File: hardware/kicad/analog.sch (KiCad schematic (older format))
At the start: 0 parts

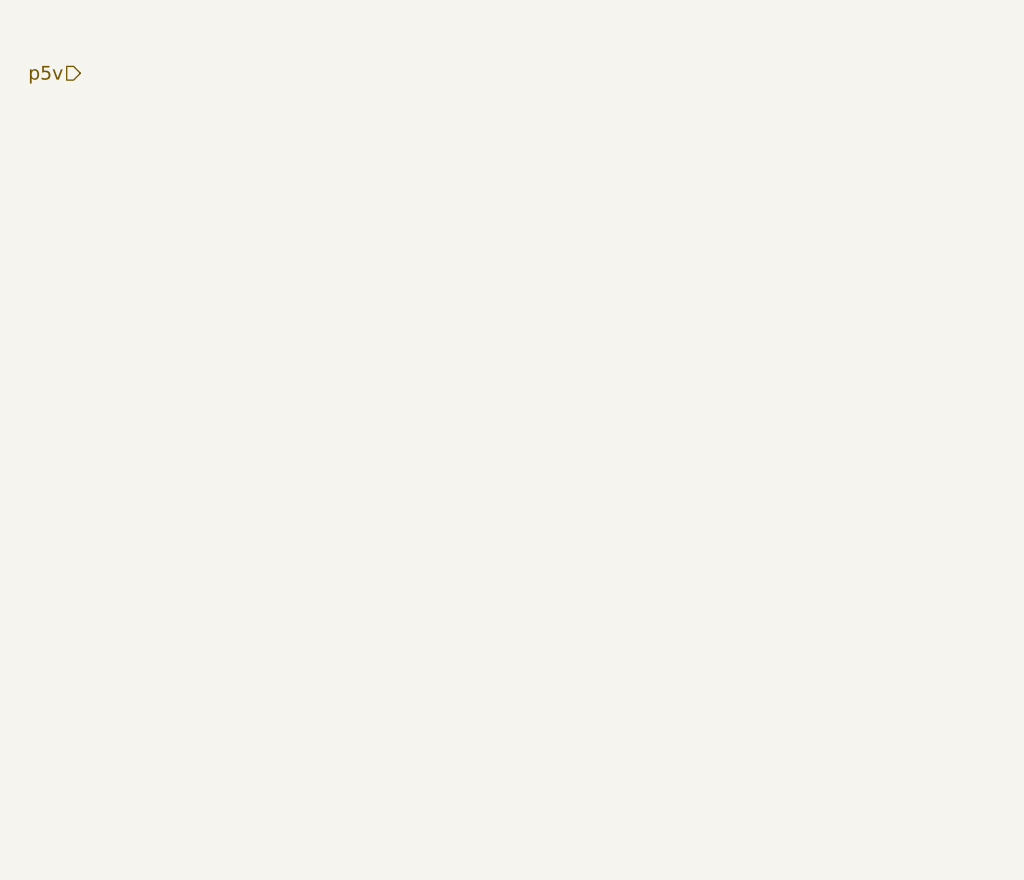
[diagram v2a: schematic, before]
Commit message: Updated schematic and Modex library.
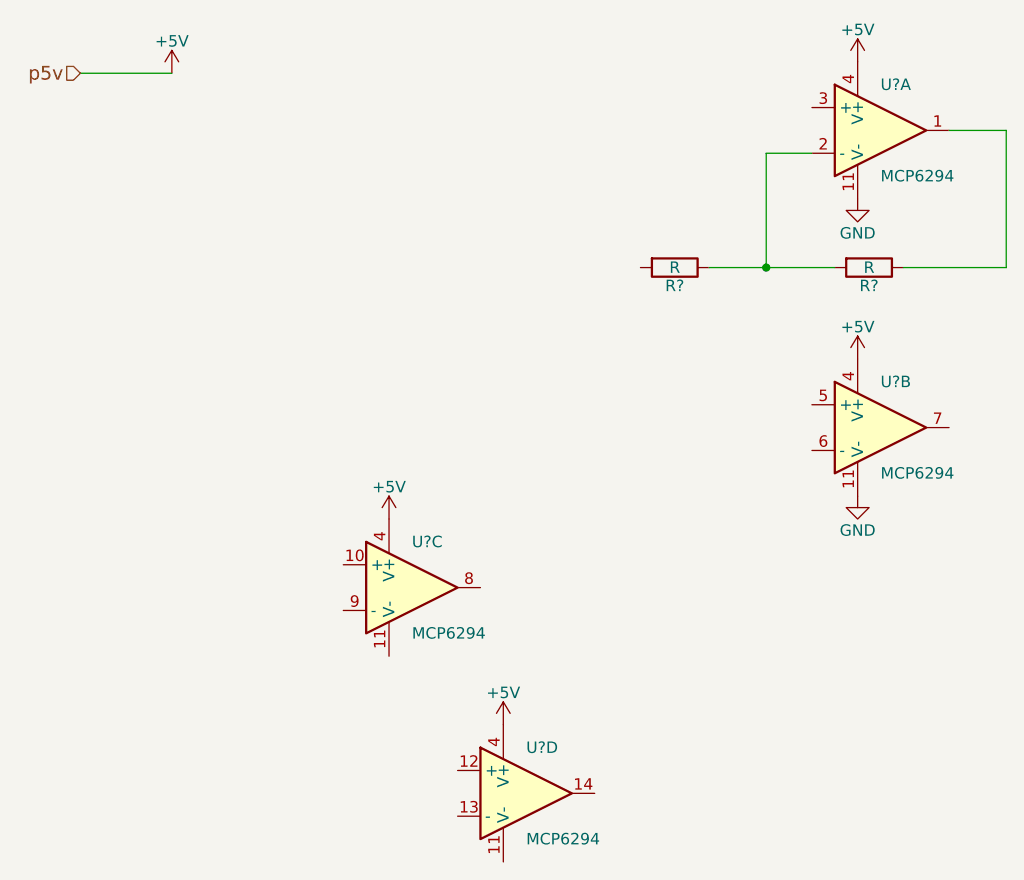
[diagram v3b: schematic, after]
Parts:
- added R? (x2): R, symbol R
- added U?: MCP6294, SMD_Packages:SO-16-N, symbol MCP6294
- added U? (x3): MCP6294, symbol MCP6294
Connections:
- new net: R?.1, U?.1
- new net: R?.1, R?.2, U?.2 (-)
- new net +5V: U?.4 (V+), U?.4 (V+), U?.4 (V+), U?.4 (V+)
- new net GND: U?.11 (V-), U?.11 (V-)
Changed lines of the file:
@@
 Text HLabel 2350 1750 0    60   Input ~ 0
 p5v
+$Comp
+L MCP6294 U?
+U 1 1 5803942A
+P 5850 2000
+F 0 "U?" H 5850 2200 50  0000 L CNN
+F 1 "MCP6294" H 5850 1800 50  0000 L CNN
+F 2 "SMD_Packages:SO-16-N" H 6500 2250 50  0001 C CNN
+F 3 "" H 5900 2200 50  0000 C CNN
+	1    5850 2000
+	1    0    0    -1
+$EndComp
+$Comp
+L MCP6294 U?
+U 2 1 58039522
+P 5850 3300
+F 0 "U?" H 5850 3500 50  0000 L CNN
+F 1 "MCP6294" H 5850 3100 50  0000 L CNN
+F 2 "" H 5800 3400 50  0000 C CNN
+F 3 "" H 5900 3500 50  0000 C CNN
+	2    5850 3300
+	1    0    0    -1
+$EndComp
+$Comp
+L MCP6294 U?
+U 3 1 58039575
+P 3800 4000
+F 0 "U?" H 3800 4200 50  0000 L CNN
+F 1 "MCP6294" H 3800 3800 50  0000 L CNN
+F 2 "" H 3750 4100 50  0000 C CNN
+F 3 "" H 3850 4200 50  0000 C CNN
+	3    3800 4000
+	1    0    0    -1
+$EndComp
+$Comp
+L MCP6294 U?
+U 4 1 580395B2
+P 4300 4900
+F 0 "U?" H 4300 5100 50  0000 L CNN
+F 1 "MCP6294" H 4300 4700 50  0000 L CNN
+F 2 "" H 4250 5000 50  0000 C CNN
+F 3 "" H 4350 5100 50  0000 C CNN
+	4    4300 4900
+	1    0    0    -1
+$EndComp
+$Comp
+L R R?
+U 1 1 58039C03
+P 5800 2600
+F 0 "R?" V 5880 2600 50  0000 C CNN
+F 1 "R" V 5800 2600 50  0000 C CNN
+F 2 "" V 5730 2600 50  0000 C CNN
+F 3 "" H 5800 2600 50  0000 C CNN
+	1    5800 2600
+	0    1    1    0
+$EndComp
+$Comp
+L R R?
+U 1 1 58039CAC
+P 4950 2600
+F 0 "R?" V 5030 2600 50  0000 C CNN
+F 1 "R" V 4950 2600 50  0000 C CNN
+F 2 "" V 4880 2600 50  0000 C CNN
+F 3 "" H 4950 2600 50  0000 C CNN
+	1    4950 2600
+	0    1    1    0
+$EndComp
+Wire Wire Line
+	5550 2100 5350 2100
+$Comp
+L GND #PWR?
+U 1 1 58039D64
+P 5750 2300
+F 0 "#PWR?" H 5750 2050 50  0001 C CNN
+F 1 "GND" H 5750 2150 50  0000 C CNN
+F 2 "" H 5750 2300 50  0000 C CNN
+F 3 "" H 5750 2300 50  0000 C CNN
+	1    5750 2300
+	1    0    0    -1
+$EndComp
+Wire Wire Line
+	5350 2100 5350 2600
+Wire Wire Line
+	5100 2600 5650 2600
+Connection ~ 5350 2600
+Wire Wire Line
+	5950 2600 6400 2600
+Wire Wire Line
+	6400 2600 6400 2000
+Wire Wire Line
+	6400 2000 6150 2000
+$Comp
+L +5V #PWR?
+U 1 1 58039E94
+P 5750 1700
+F 0 "#PWR?" H 5750 1550 50  0001 C CNN
+F 1 "+5V" H 5750 1840 50  0000 C CNN
+F 2 "" H 5750 1700 50  0000 C CNN
+F 3 "" H 5750 1700 50  0000 C CNN
+	1    5750 1700
+	1    0    0    -1
+$EndComp
+$Comp
+L +5V #PWR?
+U 1 1 58039ECC
+P 2750 1750
+F 0 "#PWR?" H 2750 1600 50  0001 C CNN
+F 1 "+5V" H 2750 1890 50  0000 C CNN
+F 2 "" H 2750 1750 50  0000 C CNN
+F 3 "" H 2750 1750 50  0000 C CNN
+	1    2750 1750
+	1    0    0    -1
+$EndComp
+Wire Wire Line
+	2350 1750 2750 1750
+$Comp
+L +5V #PWR?
+U 1 1 58039F89
+P 5750 3000
+F 0 "#PWR?" H 5750 2850 50  0001 C CNN
+F 1 "+5V" H 5750 3140 50  0000 C CNN
+F 2 "" H 5750 3000 50  0000 C CNN
+F 3 "" H 5750 3000 50  0000 C CNN
+	1    5750 3000
+	1    0    0    -1
+$EndComp
+$Comp
+L +5V #PWR?
+U 1 1 58039FB2
+P 3700 3700
+F 0 "#PWR?" H 3700 3550 50  0001 C CNN
+F 1 "+5V" H 3700 3840 50  0000 C CNN
+F 2 "" H 3700 3700 50  0000 C CNN
+F 3 "" H 3700 3700 50  0000 C CNN
+	1    3700 3700
+	1    0    0    -1
+$EndComp
+$Comp
+L +5V #PWR?
+U 1 1 5803A02F
+P 4200 4600
+F 0 "#PWR?" H 4200 4450 50  0001 C CNN
+F 1 "+5V" H 4200 4740 50  0000 C CNN
+F 2 "" H 4200 4600 50  0000 C CNN
+F 3 "" H 4200 4600 50  0000 C CNN
+	1    4200 4600
+	1    0    0    -1
+$EndComp
+$Comp
+L GND #PWR?
+U 1 1 5803A154
+P 5750 3600
+F 0 "#PWR?" H 5750 3350 50  0001 C CNN
+F 1 "GND" H 5750 3450 50  0000 C CNN
+F 2 "" H 5750 3600 50  0000 C CNN
+F 3 "" H 5750 3600 50  0000 C CNN
+	1    5750 3600
+	1    0    0    -1
+$EndComp
 $EndSCHEMATC

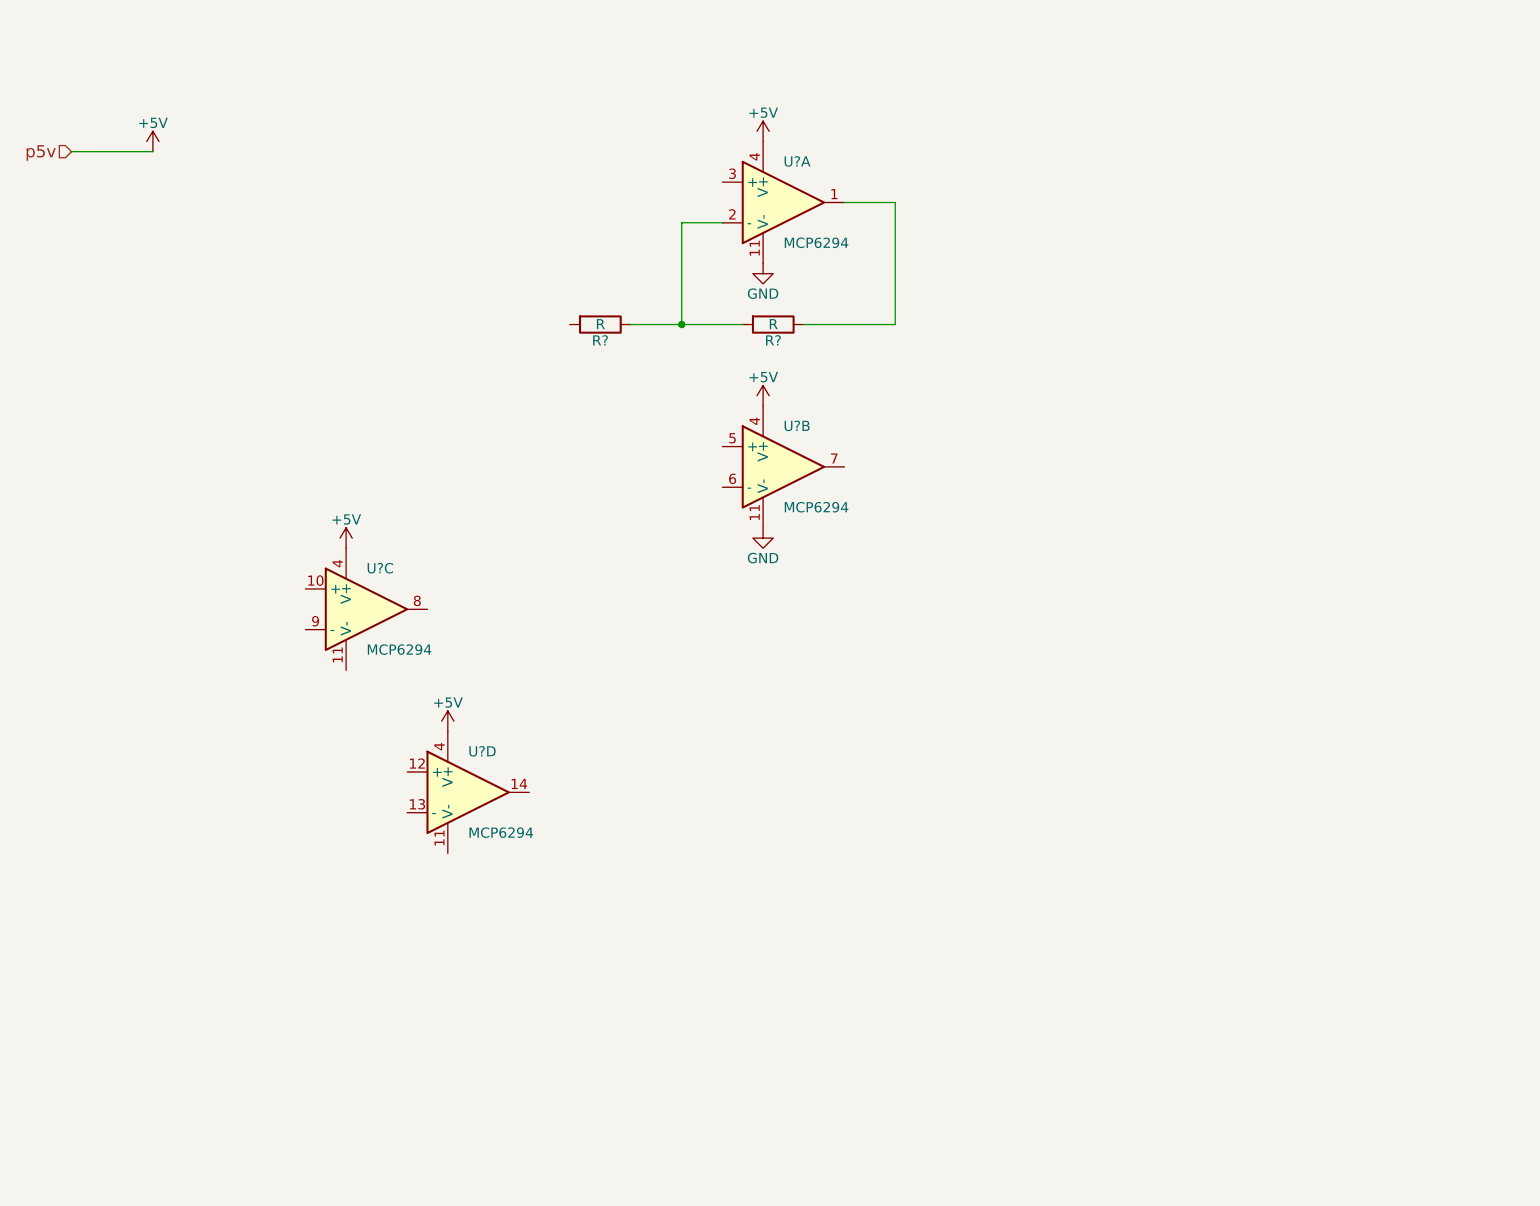
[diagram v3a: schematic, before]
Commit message: Added LTSPICE project for piezo acoustics.
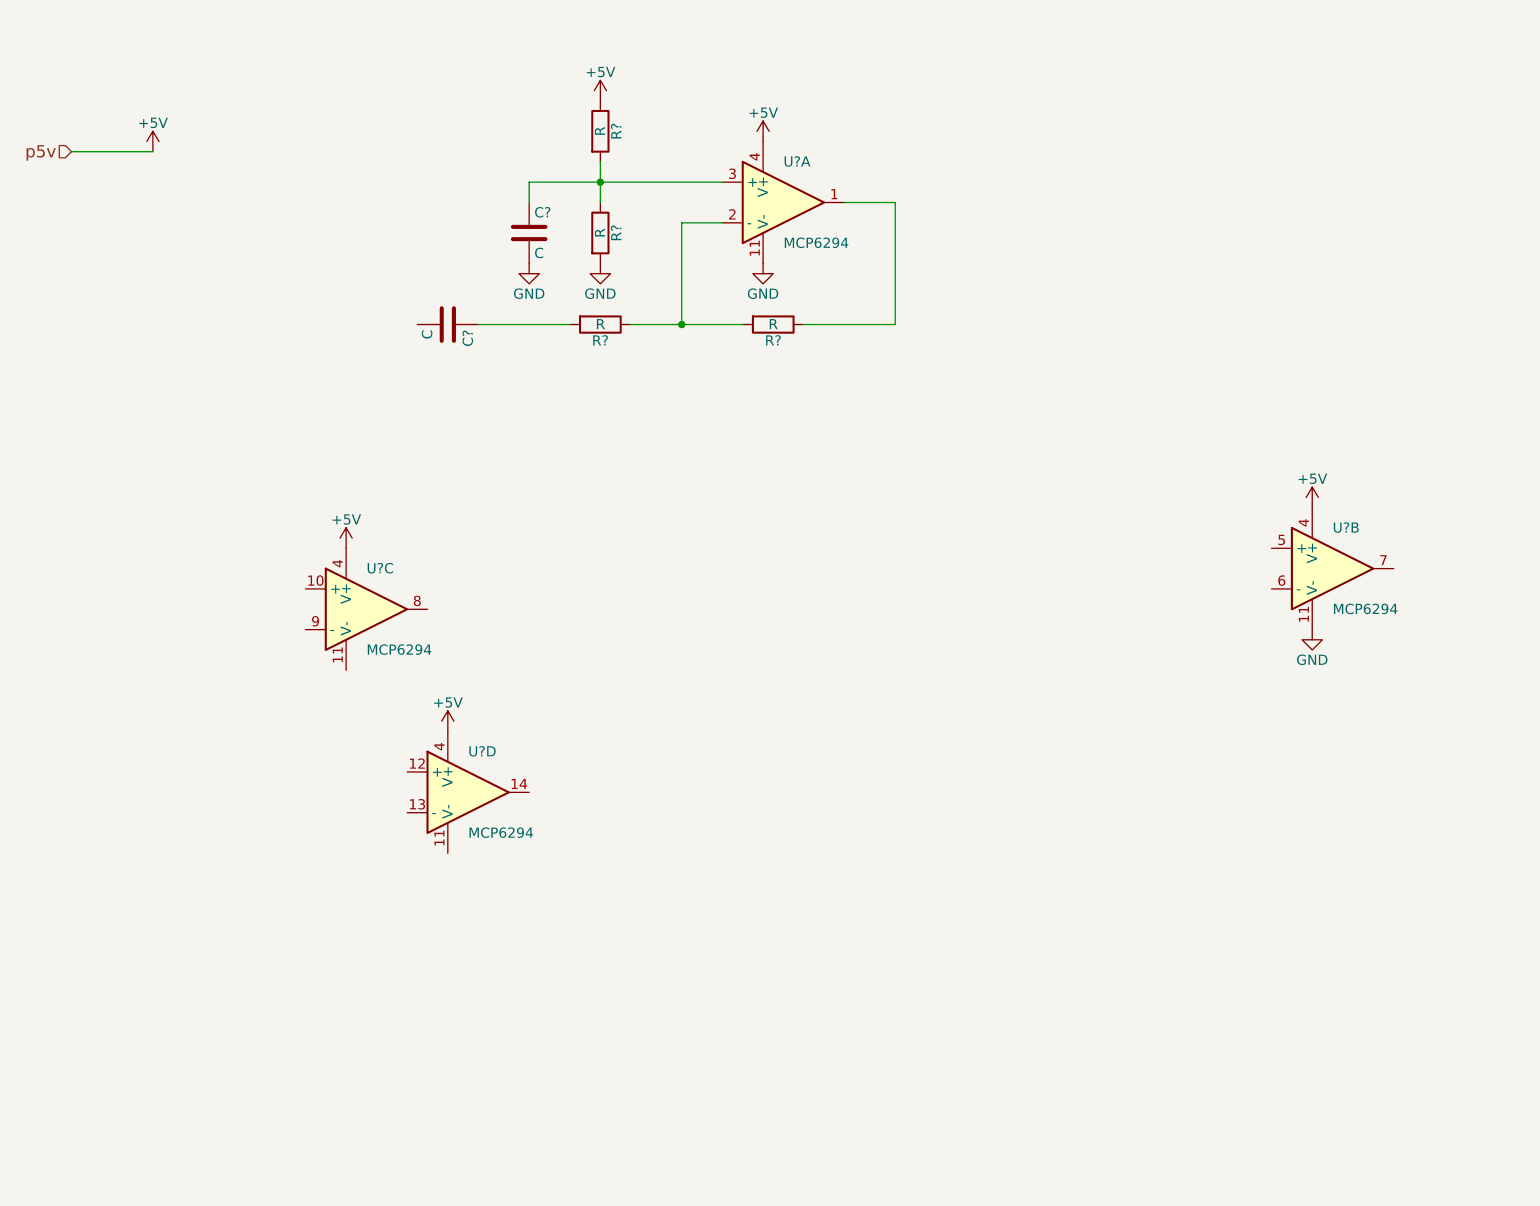
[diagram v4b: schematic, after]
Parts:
- added C? (x2): C, symbol C
- added R? (x2): R, symbol R
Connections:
- net +5V: now also R?.1
- net GND: now also C?.2, R?.2
- net at U?.3 (+): now also C?.1, R?.1, R?.2
- net at R?.2: now also C?.1
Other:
- moved on the sheet: U?B
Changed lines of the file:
@@
 L MCP6294 U?
 U 2 1 58039522
-P 5850 3300
-F 0 "U?" H 5850 3500 50  0000 L CNN
-F 1 "MCP6294" H 5850 3100 50  0000 L CNN
-F 2 "" H 5800 3400 50  0000 C CNN
-F 3 "" H 5900 3500 50  0000 C CNN
-	2    5850 3300
+P 8550 3800
+F 0 "U?" H 8550 4000 50  0000 L CNN
+F 1 "MCP6294" H 8550 3600 50  0000 L CNN
+F 2 "" H 8500 3900 50  0000 C CNN
+F 3 "" H 8600 4000 50  0000 C CNN
+	2    8550 3800
 	1    0    0    -1
 $EndComp
@@
 L +5V #PWR?
 U 1 1 58039F89
-P 5750 3000
-F 0 "#PWR?" H 5750 2850 50  0001 C CNN
-F 1 "+5V" H 5750 3140 50  0000 C CNN
-F 2 "" H 5750 3000 50  0000 C CNN
-F 3 "" H 5750 3000 50  0000 C CNN
-	1    5750 3000
+P 8450 3500
+F 0 "#PWR?" H 8450 3350 50  0001 C CNN
+F 1 "+5V" H 8450 3640 50  0000 C CNN
+F 2 "" H 8450 3500 50  0000 C CNN
+F 3 "" H 8450 3500 50  0000 C CNN
+	1    8450 3500
 	1    0    0    -1
 $EndComp
@@
 L GND #PWR?
 U 1 1 5803A154
-P 5750 3600
-F 0 "#PWR?" H 5750 3350 50  0001 C CNN
-F 1 "GND" H 5750 3450 50  0000 C CNN
-F 2 "" H 5750 3600 50  0000 C CNN
-F 3 "" H 5750 3600 50  0000 C CNN
-	1    5750 3600
-	1    0    0    -1
-$EndComp
+P 8450 4100
+F 0 "#PWR?" H 8450 3850 50  0001 C CNN
+F 1 "GND" H 8450 3950 50  0000 C CNN
+F 2 "" H 8450 4100 50  0000 C CNN
+F 3 "" H 8450 4100 50  0000 C CNN
+	1    8450 4100
+	1    0    0    -1
+$EndComp
+$Comp
+L R R?
+U 1 1 5803C9FB
+P 4950 1650
+F 0 "R?" V 5030 1650 50  0000 C CNN
+F 1 "R" V 4950 1650 50  0000 C CNN
+F 2 "" V 4880 1650 50  0000 C CNN
+F 3 "" H 4950 1650 50  0000 C CNN
+	1    4950 1650
+	1    0    0    -1
+$EndComp
+$Comp
+L R R?
+U 1 1 5803CA7A
+P 4950 2150
+F 0 "R?" V 5030 2150 50  0000 C CNN
+F 1 "R" V 4950 2150 50  0000 C CNN
+F 2 "" V 4880 2150 50  0000 C CNN
+F 3 "" H 4950 2150 50  0000 C CNN
+	1    4950 2150
+	1    0    0    -1
+$EndComp
+Wire Wire Line
+	4600 1900 5550 1900
+Connection ~ 4950 1900
+$Comp
+L +5V #PWR?
+U 1 1 5803CB06
+P 4950 1500
+F 0 "#PWR?" H 4950 1350 50  0001 C CNN
+F 1 "+5V" H 4950 1640 50  0000 C CNN
+F 2 "" H 4950 1500 50  0000 C CNN
+F 3 "" H 4950 1500 50  0000 C CNN
+	1    4950 1500
+	1    0    0    -1
+$EndComp
+$Comp
+L GND #PWR?
+U 1 1 5803CB29
+P 4950 2300
+F 0 "#PWR?" H 4950 2050 50  0001 C CNN
+F 1 "GND" H 4950 2150 50  0000 C CNN
+F 2 "" H 4950 2300 50  0000 C CNN
+F 3 "" H 4950 2300 50  0000 C CNN
+	1    4950 2300
+	1    0    0    -1
+$EndComp
+$Comp
+L C C?
+U 1 1 5803CB46
+P 4200 2600
+F 0 "C?" H 4225 2700 50  0000 L CNN
+F 1 "C" H 4225 2500 50  0000 L CNN
+F 2 "" H 4238 2450 50  0000 C CNN
+F 3 "" H 4200 2600 50  0000 C CNN
+	1    4200 2600
+	0    1    1    0
+$EndComp
+Wire Wire Line
+	4350 2600 4800 2600
+$Comp
+L C C?
+U 1 1 5803CBBF
+P 4600 2150
+F 0 "C?" H 4625 2250 50  0000 L CNN
+F 1 "C" H 4625 2050 50  0000 L CNN
+F 2 "" H 4638 2000 50  0000 C CNN
+F 3 "" H 4600 2150 50  0000 C CNN
+	1    4600 2150
+	1    0    0    -1
+$EndComp
+Wire Wire Line
+	4600 2000 4600 1900
+$Comp
+L GND #PWR?
+U 1 1 5803CC52
+P 4600 2300
+F 0 "#PWR?" H 4600 2050 50  0001 C CNN
+F 1 "GND" H 4600 2150 50  0000 C CNN
+F 2 "" H 4600 2300 50  0000 C CNN
+F 3 "" H 4600 2300 50  0000 C CNN
+	1    4600 2300
+	1    0    0    -1
+$EndComp
+Wire Wire Line
+	4950 1800 4950 2000
 $EndSCHEMATC
